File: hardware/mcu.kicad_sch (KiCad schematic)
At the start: 15 parts, among them SW2 RST, U4 ECS-327TXO-2012, U5 ATSAMD21G18A-A

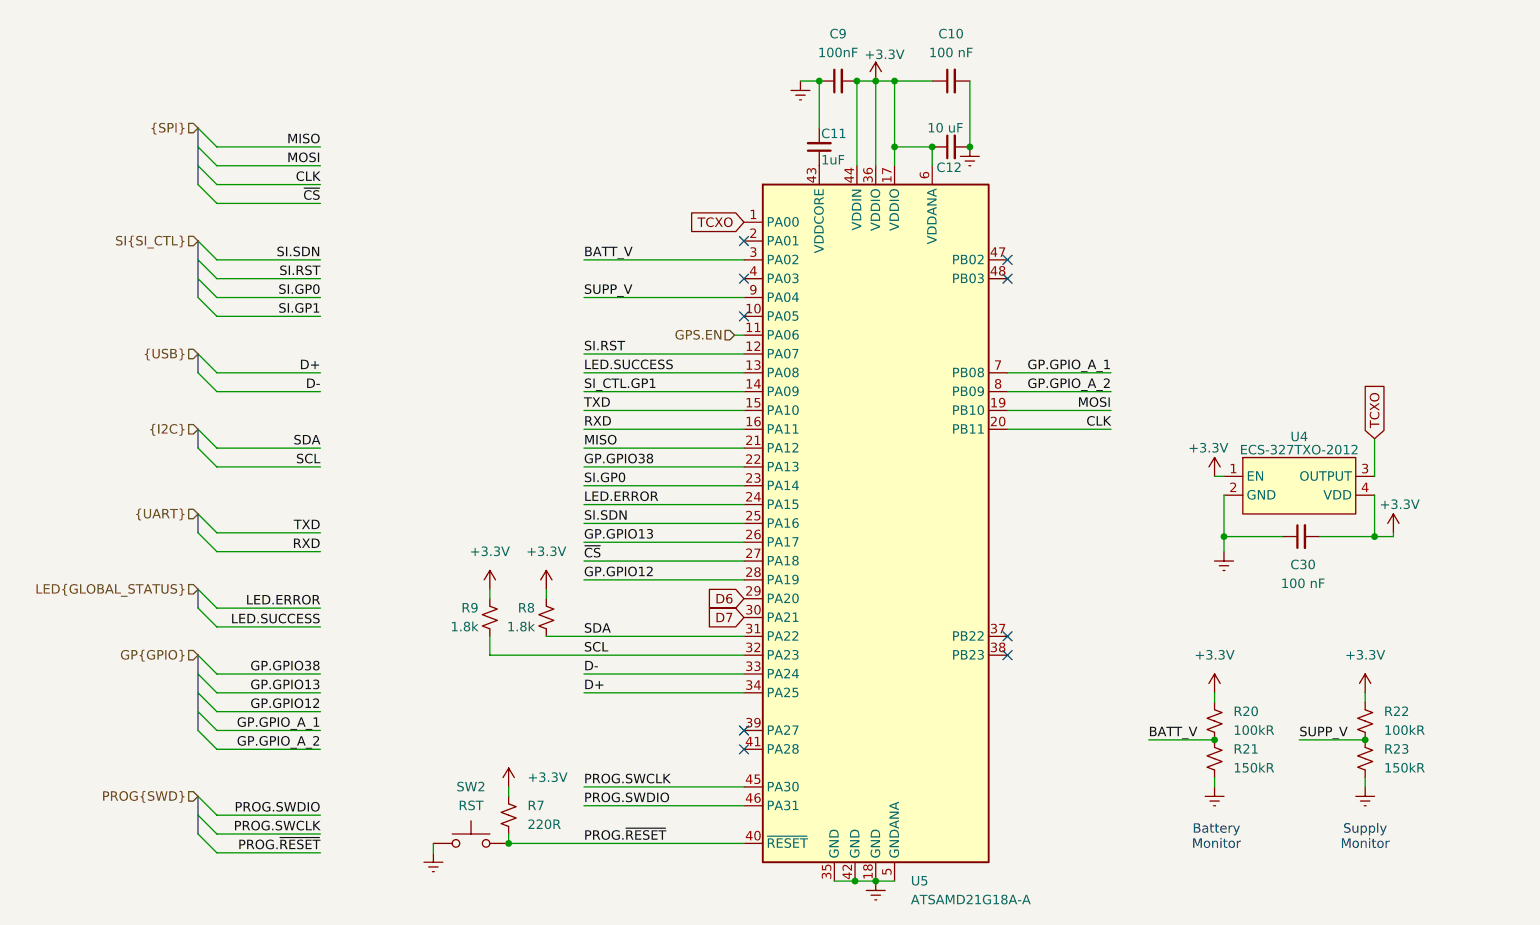
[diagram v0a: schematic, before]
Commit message: power path and bme280 fix
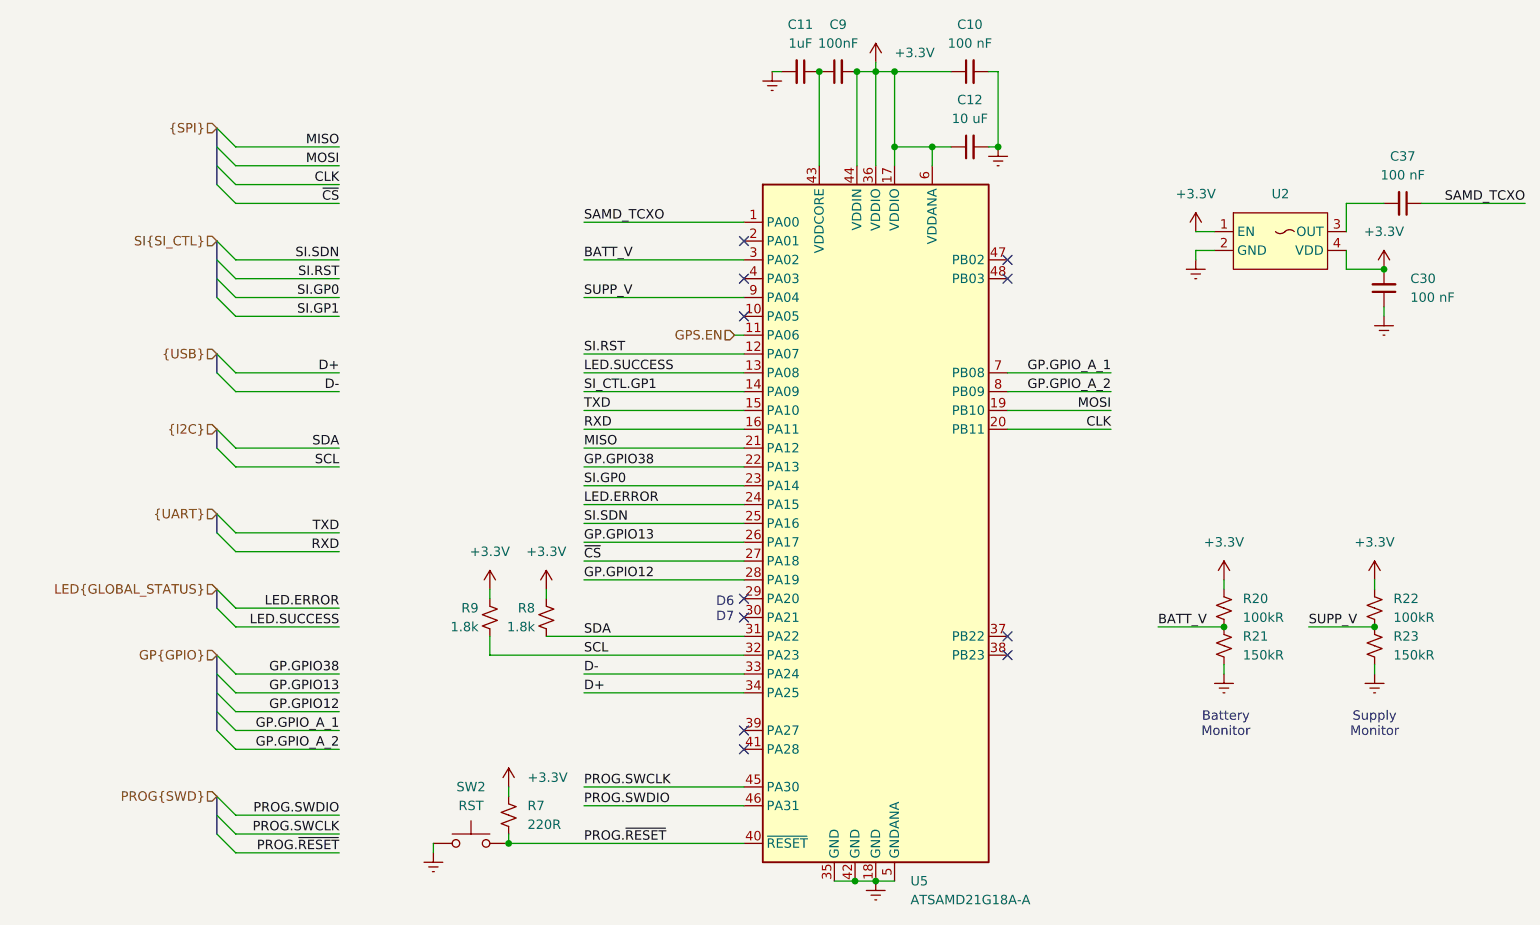
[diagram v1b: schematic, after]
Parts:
- removed U4: ECS-327TXO-2012, Crystal:Crystal_SMD_3225-4Pin_3.2x2.5mm, symbol Oscillator:ATXK-H11-E-32.768KHZ-E50-T3
- added C37: 100 nF, Capacitor_SMD:C_0402_1005Metric_Pad0.74x0.62mm_HandSolder, symbol Device:C_Small
- added U2: (no value), symbol Oscillator_Custom:Device_TCXO_EN
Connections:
- net +3.3V: now also U2.1 (EN), U2.4 (VDD)
- net Earth: now also U2.2 (GND); no longer C9.1
- net at C11.1, U5.43 (VDDCORE): now also C9.1
- net D6: no longer names the net of U5.29 (PA20)
- net D7: no longer names the net of U5.30 (PA21)
- net TCXO renamed SAMD_TCXO
- net SAMD_TCXO: now also C37.1
- new net: C37.2, U2.3 (OUT)
- no-connect marks 9 -> 11
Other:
- note added: "D6 D7"
- moved on the sheet: C10, C11, C12, C30, C9, R20, R21, R22, R23

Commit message: pcb rework -- layout subsections and rough floorplanning
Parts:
- C10, C30, C37: value 100 nF -> 100nF; footprint Capacitor_SMD:C_0402_1005Metric_Pad0.74x0.62mm_HandSolder -> Capacitor_SMD:C_0402_1005Metric
- C11, C9: footprint Capacitor_SMD:C_0402_1005Metric_Pad0.74x0.62mm_HandSolder -> Capacitor_SMD:C_0402_1005Metric
- C12: value 10 uF -> 10uF; footprint Capacitor_SMD:C_0402_1005Metric_Pad0.74x0.62mm_HandSolder -> Capacitor_SMD:C_0402_1005Metric
- R20, R21, R22, R23: footprint Resistor_SMD:R_0402_1005Metric_Pad0.72x0.64mm_HandSolder -> Capacitor_SMD:C_0402_1005Metric
- R7: footprint Resistor_SMD:R_0402_1005Metric_Pad0.72x0.64mm_HandSolder -> Resistor_SMD:R_0402_1005Metric
- R8, R9: value 1.8k -> 1.8kR; footprint Resistor_SMD:R_0402_1005Metric_Pad0.72x0.64mm_HandSolder -> Resistor_SMD:R_0402_1005Metric
- U2: footprint (none) -> Crystal:Crystal_SMD_2016-4Pin_2.0x1.6mm
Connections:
- net +3.3V: no longer R20.1
- new net +BATT: R20.1

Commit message: draft of final layout
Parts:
- SW2: footprint Button_Switch_SMD:SW_Tactile_SPST_NO_Straight_CK_PTS636Sx25SMTRLFS -> Button_Switch_SMD:SW_SPST_TS-1088-xR020
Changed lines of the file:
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@@
 			)
 		)
-		(property "Footprint" "Button_Switch_SMD:SW_Tactile_SPST_NO_Straight_CK_PTS636Sx25SMTRLFS"
+		(property "Footprint" "Button_Switch_SMD:SW_SPST_TS-1088-xR020"
 			(at 114.3 132.08 0)
 			(hide yes)

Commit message: net class shenanigans
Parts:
- C10, C11, C12, C30, C37, C9, R20, R21, R22, R23, R7, R8, R9: KiLib_Generator (none) -> SMD_2terminal_chip_molded
- U2: KiLib_Generator (none) -> crystal_resonator_oscillator
- U5: KiLib_Generator (none) -> package/gullwing
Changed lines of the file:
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@@
 			)
 		)
+		(property "KiLib_Generator" "SMD_2terminal_chip_molded"
+			(at 240.03 50.8 0)
+			(hide yes)
+			(show_name no)
+			(do_not_autoplace no)
+			(effects
+				(font
+					(size 1.27 1.27)
+				)
+			)
+		)
 		(pin "1"
 		)
@@
 			)
 		)
+		(property "KiLib_Generator" "SMD_2terminal_chip_molded"
+			(at 236.22 110.49 0)
+			(hide yes)
+			(show_name no)
+			(do_not_autoplace no)
+			(effects
+				(font
+					(size 1.27 1.27)
+				)
+			)
+		)
 		(pin "1"
 		)
@@
 			)
 		)
+		(property "KiLib_Generator" "SMD_2terminal_chip_molded"
+			(at 215.9 105.41 0)
+			(hide yes)
+			(show_name no)
+			(do_not_autoplace no)
+			(effects
+				(font
+					(size 1.27 1.27)
+				)
+			)
+		)
 		(pin "1"
 		)
@@
 			)
 		)
+		(property "KiLib_Generator" "SMD_2terminal_chip_molded"
+			(at 237.49 62.23 0)
+			(hide yes)
+			(show_name no)
+			(do_not_autoplace no)
+			(effects
+				(font
+					(size 1.27 1.27)
+				)
+			)
+		)
 		(pin "1"
 		)
@@
 			)
 		)
+		(property "KiLib_Generator" "SMD_2terminal_chip_molded"
+			(at 124.46 106.68 0)
+			(hide yes)
+			(show_name no)
+			(do_not_autoplace no)
+			(effects
+				(font
+					(size 1.27 1.27)
+				)
+			)
+		)
 		(pin "1"
 		)
@@
 			)
 		)
+		(property "KiLib_Generator" "SMD_2terminal_chip_molded"
+			(at 181.61 43.18 0)
+			(hide yes)
+			(show_name no)
+			(do_not_autoplace no)
+			(effects
+				(font
+					(size 1.27 1.27)
+				)
+			)
+		)
 		(pin "1"
 		)
@@
 			)
 		)
+		(property "KiLib_Generator" "SMD_2terminal_chip_molded"
+			(at 181.61 33.02 0)
+			(hide yes)
+			(show_name no)
+			(do_not_autoplace no)
+			(effects
+				(font
+					(size 1.27 1.27)
+				)
+			)
+		)
 		(pin "1"
 		)
@@
 			)
 		)
+		(property "KiLib_Generator" "SMD_2terminal_chip_molded"
+			(at 215.9 110.49 0)
+			(hide yes)
+			(show_name no)
+			(do_not_autoplace no)
+			(effects
+				(font
+					(size 1.27 1.27)
+				)
+			)
+		)
 		(pin "1"
 		)
@@
 			)
 		)
+		(property "KiLib_Generator" "SMD_2terminal_chip_molded"
+			(at 158.75 33.02 0)
+			(hide yes)
+			(show_name no)
+			(do_not_autoplace no)
+			(effects
+				(font
+					(size 1.27 1.27)
+				)
+			)
+		)
 		(pin "1"
 		)
@@
 			)
 		)
+		(property "KiLib_Generator" "SMD_2terminal_chip_molded"
+			(at 163.83 33.02 0)
+			(hide yes)
+			(show_name no)
+			(do_not_autoplace no)
+			(effects
+				(font
+					(size 1.27 1.27)
+				)
+			)
+		)
 		(pin "1"
 		)
@@
 			)
 		)
+		(property "KiLib_Generator" "SMD_2terminal_chip_molded"
+			(at 236.22 105.41 0)
+			(hide yes)
+			(show_name no)
+			(do_not_autoplace no)
+			(effects
+				(font
+					(size 1.27 1.27)
+				)
+			)
+		)
 		(pin "1"
 		)
@@
 			)
 		)
+		(property "KiLib_Generator" "SMD_2terminal_chip_molded"
+			(at 116.84 106.68 0)
+			(hide yes)
+			(show_name no)
+			(do_not_autoplace no)
+			(effects
+				(font
+					(size 1.27 1.27)
+				)
+			)
+		)
 		(pin "1"
 		)
@@
 			)
 		)
+		(property "KiLib_Generator" "package/gullwing"
+			(at 168.91 93.98 0)
+			(hide yes)
+			(show_name no)
+			(do_not_autoplace no)
+			(effects
+				(font
+					(size 1.27 1.27)
+				)
+			)
+		)
 		(pin "1"
 		)
@@
 			)
 		)
+		(property "KiLib_Generator" "SMD_2terminal_chip_molded"
+			(at 119.38 133.35 0)
+			(hide yes)
+			(show_name no)
+			(do_not_autoplace no)
+			(effects
+				(font
+					(size 1.27 1.27)
+				)
+			)
+		)
 		(pin "1"
 		)
@@
 			(at 223.52 49.53 0)
 			(hide yes)
+			(show_name no)
+			(do_not_autoplace no)
+			(effects
+				(font
+					(size 1.27 1.27)
+				)
+			)
+		)
+		(property "KiLib_Generator" "crystal_resonator_oscillator"
+			(at 223.52 49.53 0)
+			(hide yes)

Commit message: draft of routing
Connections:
- net GP.GPIO38 is gone; now on net SI.GP0: U5.22 (PA13)
- net SI_CTL.GP1 is gone; now on net SI.GP1: U5.14 (PA09)
- net GPS.EN: now also U5.39 (PA27); no longer U5.11 (PA06)
- net LED.ERROR: now also U5.48 (PB03); no longer U5.24 (PA15)
- net LED.SUCCESS: now also U5.47 (PB02); no longer U5.13 (PA08)
- net SI.GP0: no longer U5.23 (PA14)
- net SI.SDN: now also U5.11 (PA06); no longer U5.25 (PA16)
- net ~{CS}: now also U5.13 (PA08); no longer U5.27 (PA18)
- new net GP.GPIO10: U5.27 (PA18)
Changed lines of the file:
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@@
+	)
+	(no_connect
+		(at 151.13 93.98)
+	)
+	(no_connect
+		(at 151.13 88.9)
 	)
 	(no_connect
@@
 	)
 	(no_connect
+		(at 151.13 91.44)
+	)
+	(no_connect
 		(at 151.13 104.14)
-	)
-	(no_connect
-		(at 186.69 60.96)
-	)
-	(no_connect
-		(at 186.69 58.42)
 	)
 	(no_connect
 		(at 151.13 106.68)
 	)
-	(no_connect
-		(at 151.13 121.92)
-	)
 	(bus_entry
 		(at 80.01 43.18)
@@
 	(wire
 		(pts
+			(xy 200.66 58.42) (xy 186.69 58.42)
+		)
+		(stroke
+			(width 0)
+			(type default)
+		)
+	)
+	(wire
+		(pts
 			(xy 129.54 114.3) (xy 151.13 114.3)
 		)
@@
 	(wire
 		(pts
-			(xy 149.86 68.58) (xy 151.13 68.58)
-		)
-		(stroke
-			(width 0)
-			(type default)
-		)
-	)
-	(wire
-		(pts
 			(xy 82.55 133.35) (xy 96.52 133.35)
 		)
@@
 	(wire
 		(pts
-			(xy 129.54 88.9) (xy 151.13 88.9)
-		)
-		(stroke
-			(width 0)
-			(type default)
-		)
-	)
-	(wire
-		(pts
 			(xy 200.66 76.2) (xy 186.69 76.2)
 		)
@@
 	(wire
 		(pts
-			(xy 129.54 93.98) (xy 151.13 93.98)
-		)
-		(stroke
-			(width 0)
-			(type default)
-		)
-	)
-	(wire
-		(pts
 			(xy 168.91 31.75) (xy 168.91 33.02)
 		)
@@
 	(wire
 		(pts
+			(xy 147.32 121.92) (xy 151.13 121.92)
+		)
+		(stroke
+			(width 0)
+			(type default)
+		)
+	)
+	(wire
+		(pts
 			(xy 176.53 43.18) (xy 176.53 45.72)
 		)
@@
 	(wire
 		(pts
-			(xy 129.54 91.44) (xy 151.13 91.44)
-		)
-		(stroke
-			(width 0)
-			(type default)
-		)
-	)
-	(wire
-		(pts
 			(xy 129.54 132.08) (xy 151.13 132.08)
 		)
@@
 	(wire
 		(pts
+			(xy 129.54 68.58) (xy 151.13 68.58)
+		)
+		(stroke
+			(width 0)
+			(type default)
+		)
+	)
+	(wire
+		(pts
 			(xy 82.55 76.2) (xy 96.52 76.2)
 		)
@@
 		(pts
 			(xy 119.38 135.89) (xy 119.38 137.16)
+		)
+		(stroke
+			(width 0)
+			(type default)
+		)
+	)
+	(wire
+		(pts
+			(xy 200.66 60.96) (xy 186.69 60.96)
 		)
 		(stroke
@@
 		)
 	)
-	(label "LED.SUCCESS"
-		(at 129.54 73.66 0)
-		(effects
-			(font
-				(size 1.27 1.27)
-			)
-			(justify left bottom)
-		)
-	)
 	(label "D+"
 		(at 129.54 116.84 0)
@@
 		)
 	)
-	(label "LED.ERROR"
-		(at 129.54 91.44 0)
-		(effects
-			(font
-				(size 1.27 1.27)
-			)
-			(justify left bottom)
-		)
-	)
 	(label "GP.GPIO12"
 		(at 129.54 101.6 0)
@@
 		)
 	)
-	(label "GP.GPIO38"
+	(label "GP.GPIO10"
 		(at 96.52 114.3 180)
 		(effects
@@
 			)
 			(justify right bottom)
-		)
-	)
-	(label "SI.SDN"
-		(at 129.54 93.98 0)
-		(effects
-			(font
-				(size 1.27 1.27)
-			)
-			(justify left bottom)
 		)
 	)
@@
 		)
 	)
+	(label "GP.GPIO10"
+		(at 129.54 99.06 0)
+		(effects
+			(font
+				(size 1.27 1.27)
+			)
+			(justify left bottom)
+		)
+	)
 	(label "LED.SUCCESS"
 		(at 96.52 107.95 180)
@@
 		)
 	)
+	(label "LED.SUCCESS"
+		(at 200.66 58.42 180)
+		(effects
+			(font
+				(size 1.27 1.27)
+			)
+			(justify right bottom)
+		)
+	)
 	(label "PROG.SWCLK"
 		(at 96.52 135.89 180)
@@
 		)
 	)
-	(label "SI_CTL.GP1"
+	(label "SI.GP1"
 		(at 129.54 76.2 0)
 		(effects
@@
 	)
 	(label "~{CS}"
-		(at 129.54 99.06 0)
+		(at 129.54 73.66 0)
 		(effects
 			(font
@@
 		)
 	)
+	(label "SI.SDN"
+		(at 129.54 68.58 0)
+		(effects
+			(font
+				(size 1.27 1.27)
+			)
+			(justify left bottom)
+		)
+	)
 	(label "GP.GPIO13"
 		(at 129.54 96.52 0)
@@
 		)
 	)
-	(label "GP.GPIO38"
-		(at 129.54 86.36 0)
-		(effects
-			(font
-				(size 1.27 1.27)
-			)
-			(justify left bottom)
-		)
-	)
 	(label "PROG.SWCLK"
 		(at 129.54 129.54 0)
@@
 		)
 	)
+	(label "LED.ERROR"
+		(at 200.66 60.96 180)
+		(effects
+			(font
+				(size 1.27 1.27)
+			)
+			(justify right bottom)
+		)
+	)
 	(label "SI.RST"
 		(at 129.54 71.12 0)
@@
 	)
 	(label "SI.GP0"
-		(at 129.54 88.9 0)
+		(at 129.54 86.36 0)
 		(effects
 			(font
@@
 			)
 			(justify right bottom)
-		)
-	)
-	(hierarchical_label "GPS.EN"
-		(shape input)
-		(at 149.86 68.58 180)
-		(effects
-			(font
-				(size 1.27 1.27)
-			)
-			(justify right)
 		)
 	)
@@
 		(effects
 			(font
+				(size 1.27 1.27)
+			)
+			(justify right)
+		)
+	)
+	(hierarchical_label "GPS.EN"
+		(shape input)
+		(at 147.32 121.92 180)
+		(effects
+			(font
